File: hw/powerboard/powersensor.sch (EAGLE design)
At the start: 35 parts, among them J1 ISP, J2 I2C

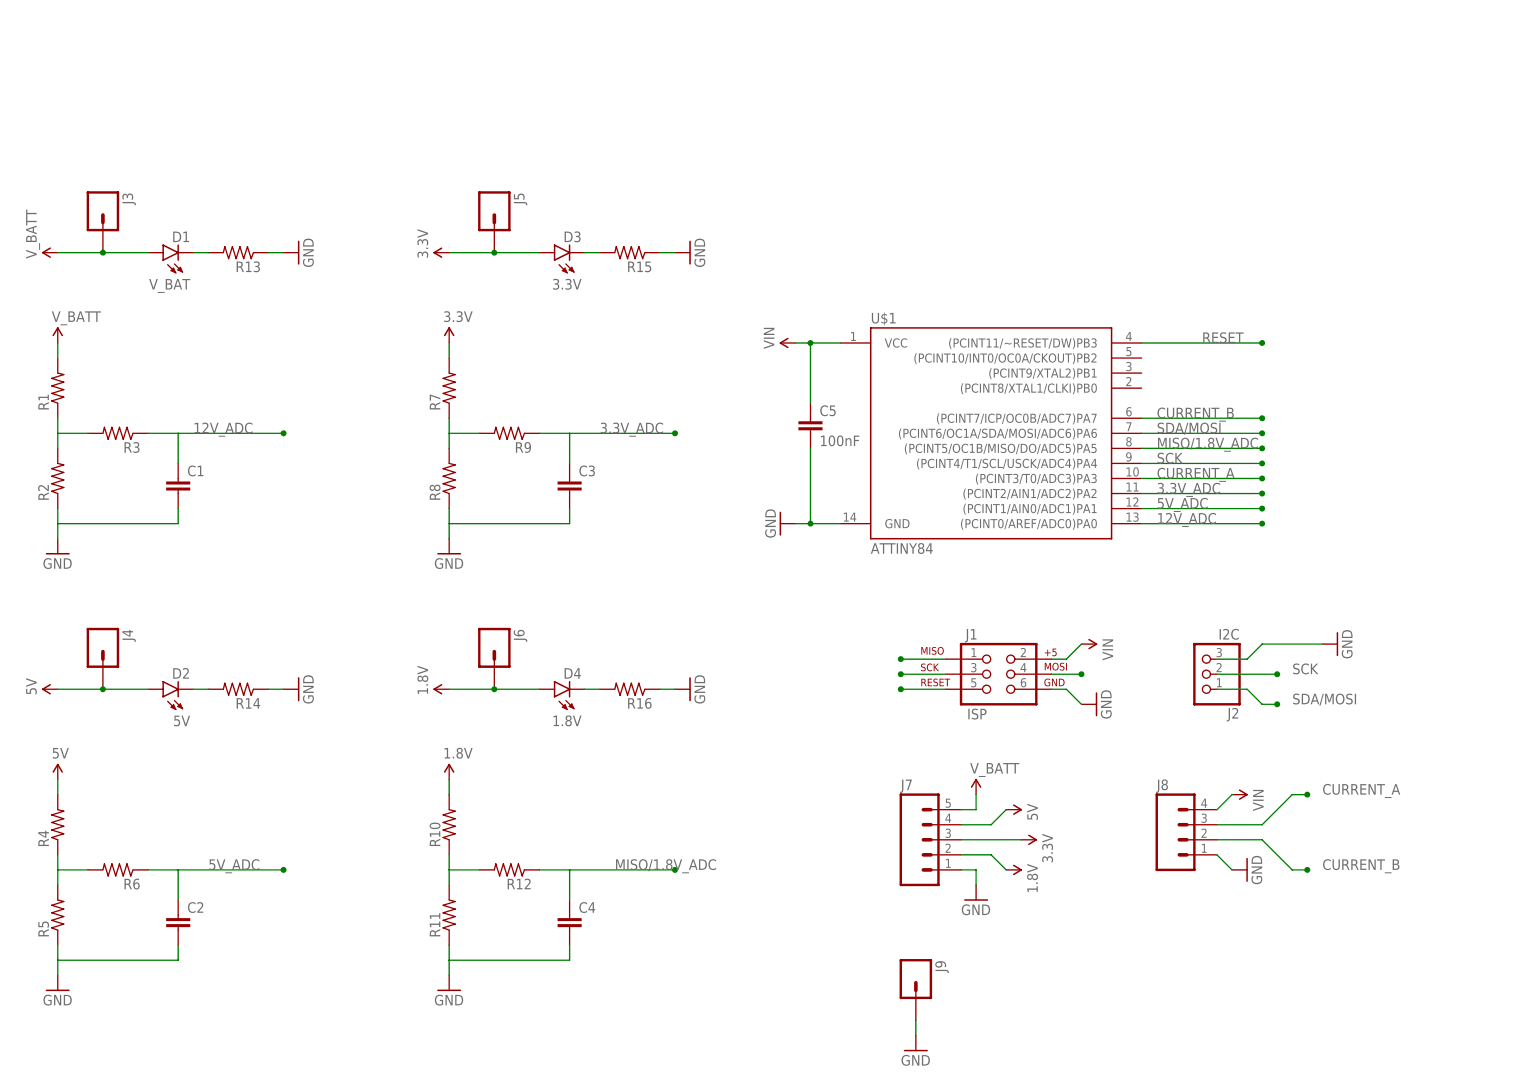
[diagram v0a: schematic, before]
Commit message: Added optional I2C pullups, broke out PB0/1 and performed some cosmetical changes to PowerSensor board
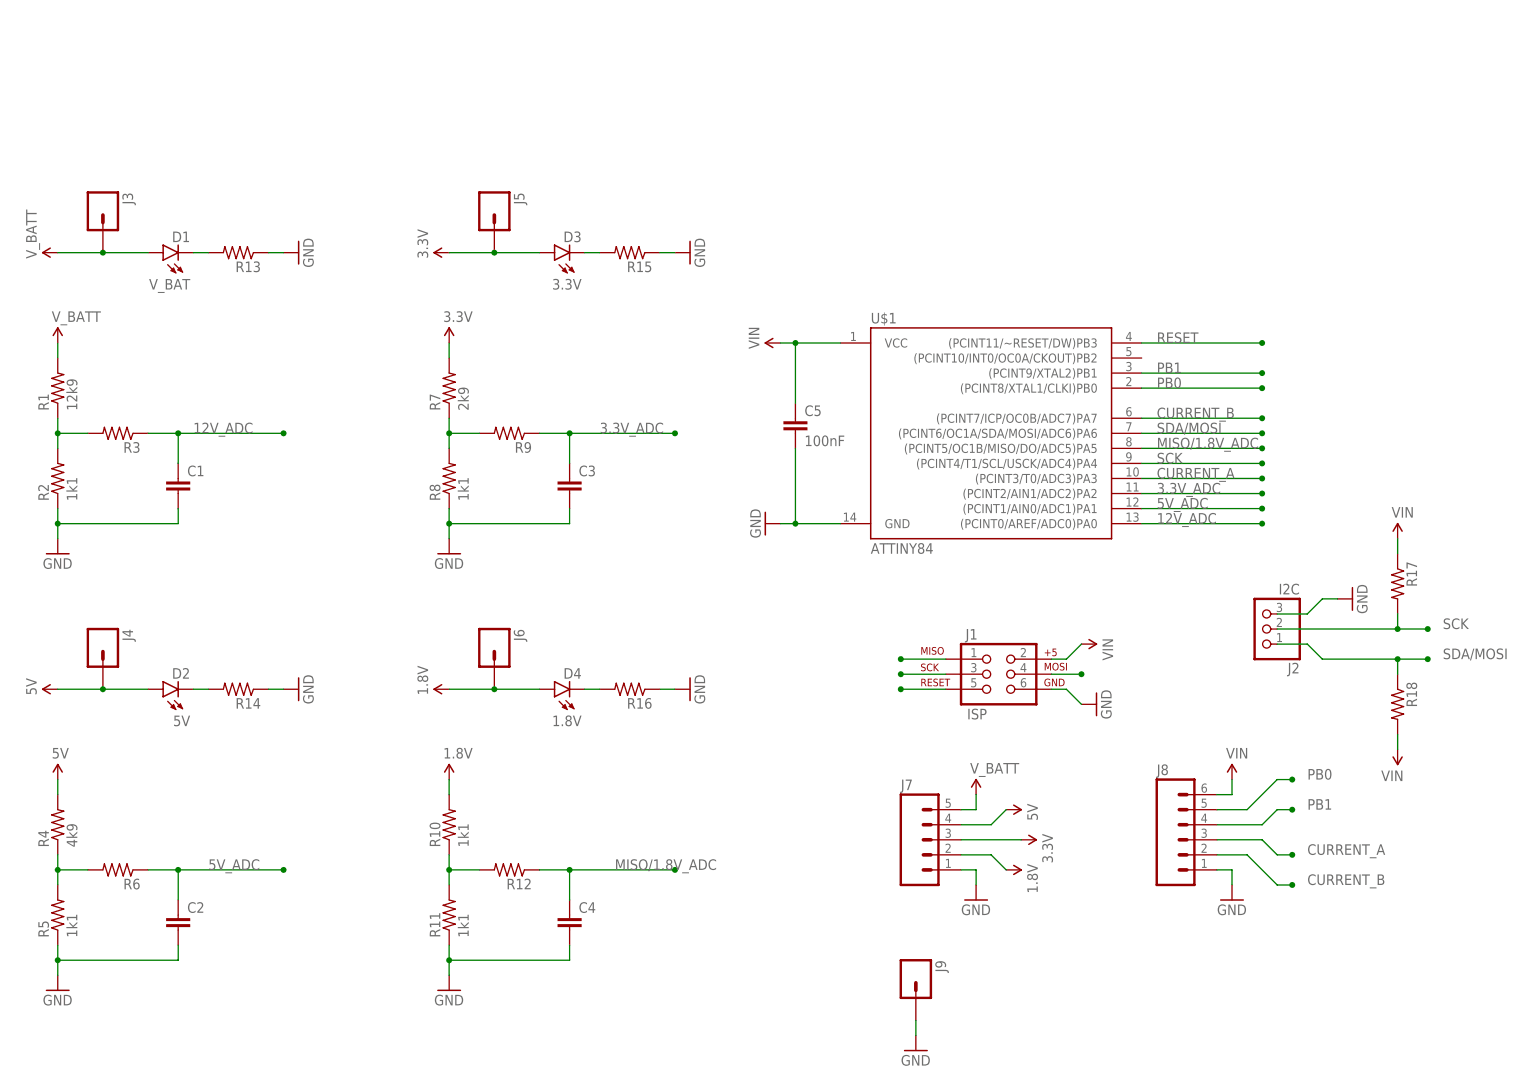
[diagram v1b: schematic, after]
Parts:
- added R17, R18: (no value), SparkFun-Passives:RESISTOR0603-RES
- J8: device SparkFun-Connectors:M04PTH -> SparkFun-Connectors:M06SILK_FEMALE_PTH
- R1: value (none) -> 12k9
- R10, R11, R2, R5, R8: value (none) -> 1k1
- R4: value (none) -> 4k9
- R7: value (none) -> 2k9
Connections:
- new net PB0: J8.5, U$1.(PCINT8/XTAL1/CLKI)PB0
- new net PB1: J8.4, U$1.(PCINT9/XTAL2)PB1
- net SCK: now also R17.2
- net SDA/MOSI: now also R18.1
- net VIN: now also J8.6, R17.1, R18.2; no longer J8.4
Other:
- moved on the sheet: C5, J2

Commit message: Added values and performed some cosmetic changes on PowerSensor schematics
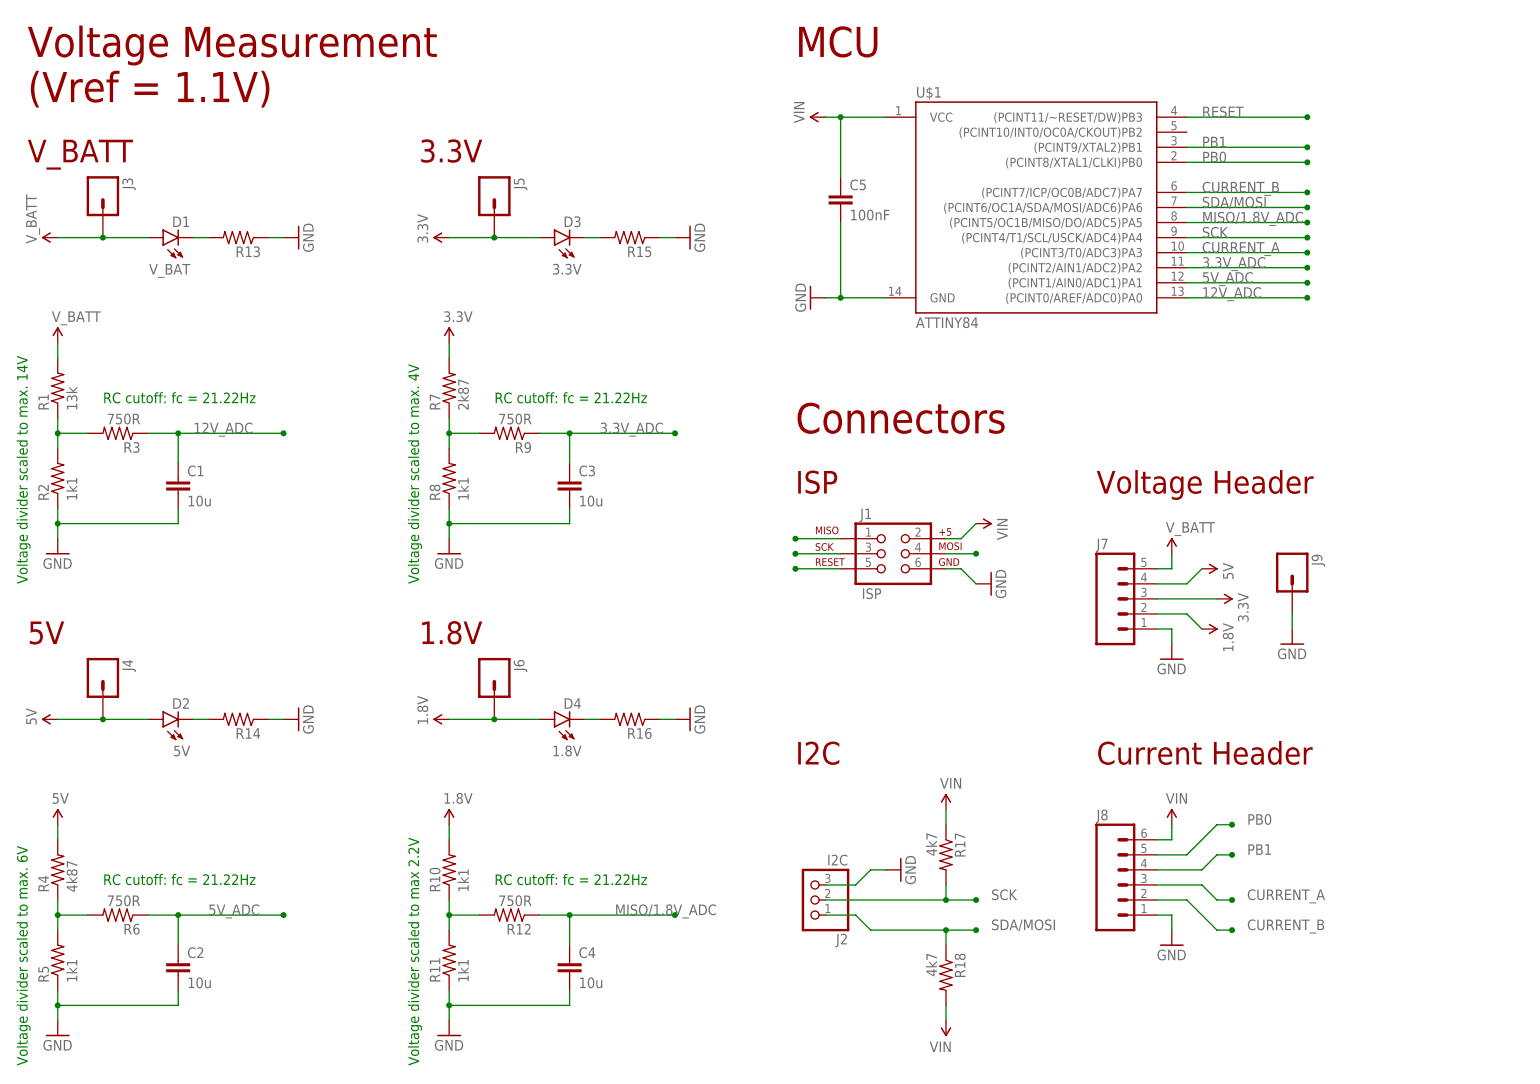
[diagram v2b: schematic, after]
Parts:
- C1, C2, C3, C4: value (none) -> 10u
- R1: value 12k9 -> 13k
- R12, R3, R6, R9: value (none) -> 750R
- R17, R18: value (none) -> 4k7
- R4: value 4k9 -> 4k87
- R7: value 2k9 -> 2k87
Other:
- note added: "1.8V"
- note added: "3.3V"
- note added: "5V"
- note added: "Connectors"
- note added: "Current Header"
- note added: "I2C"
- note added: "ISP"
- note added: "MCU"
- note added: "RC cutoff: fc = 21.22Hz"
- note added: "V_BATT"
- note added: "Voltage Header"
- note added: "Voltage Measurement (Vref = 1.1V)"
- note added: "Voltage divider scaled to max 2.2V"
- note added: "Voltage divider scaled to max. 14V"
- note added: "Voltage divider scaled to max. 4V"
- note added: "Voltage divider scaled to max. 6V"
- moved on the sheet: C2, C4, C5, D1, D2, D3, D4, J1, J2, J3, J4, J5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

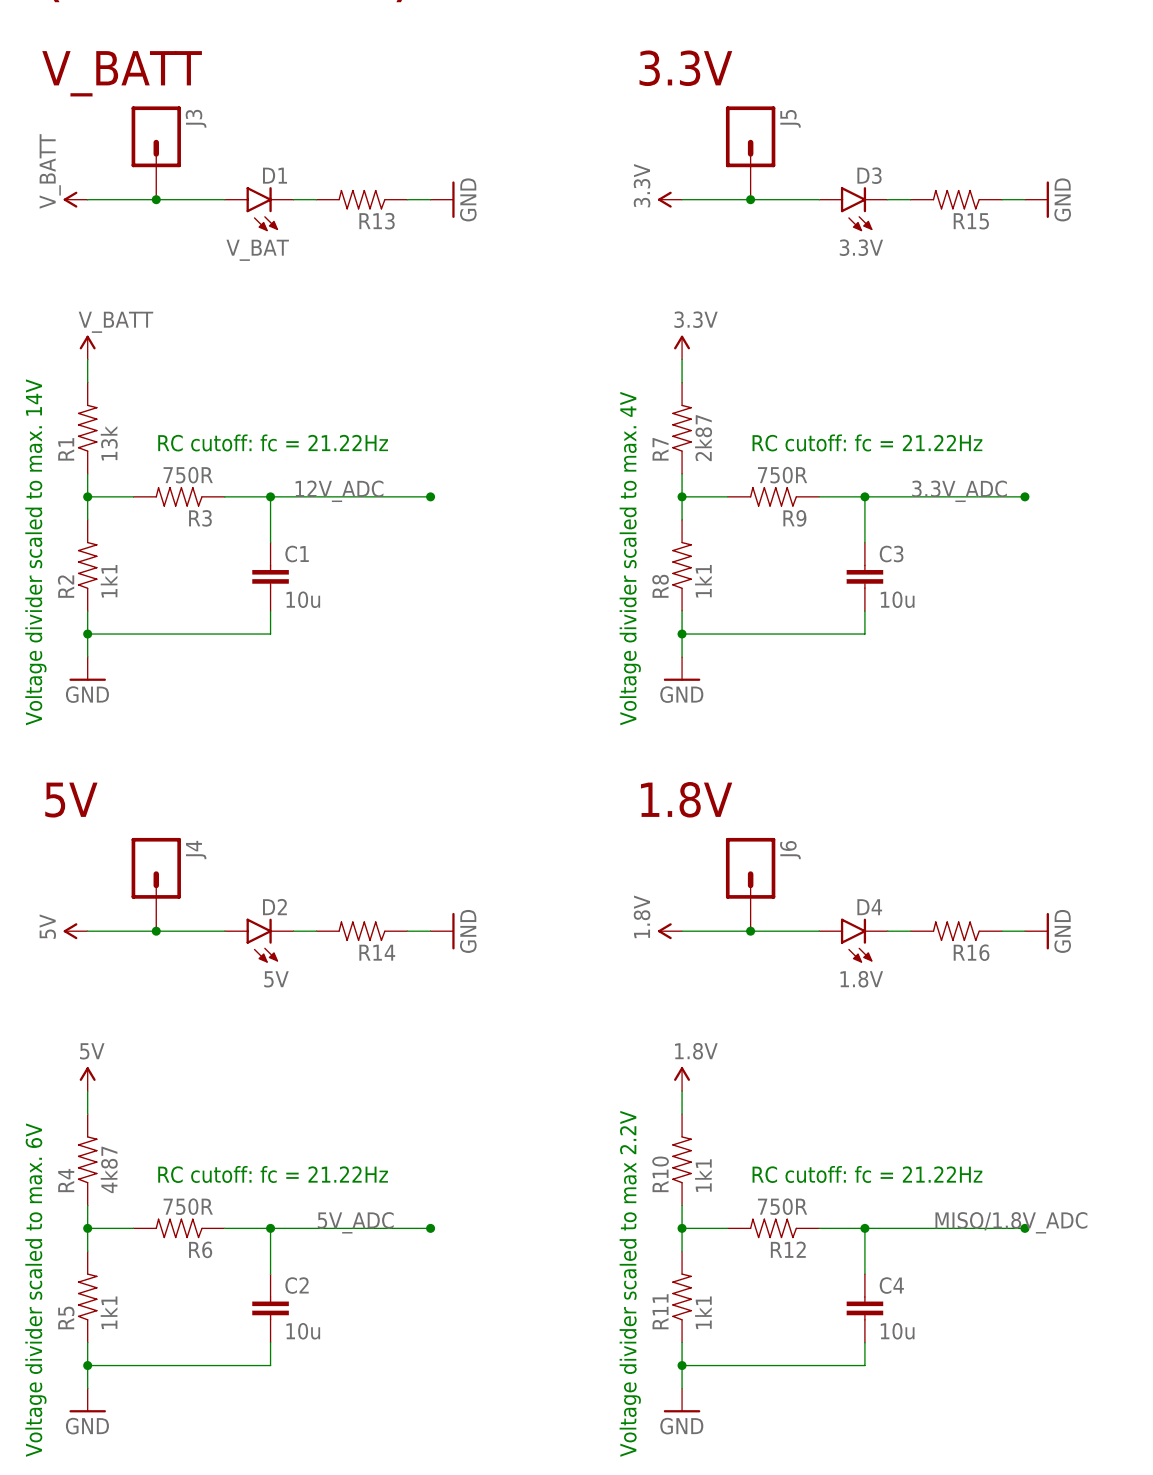
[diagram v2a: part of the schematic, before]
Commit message: Fixed values and added product ids for PowerSensor BOM
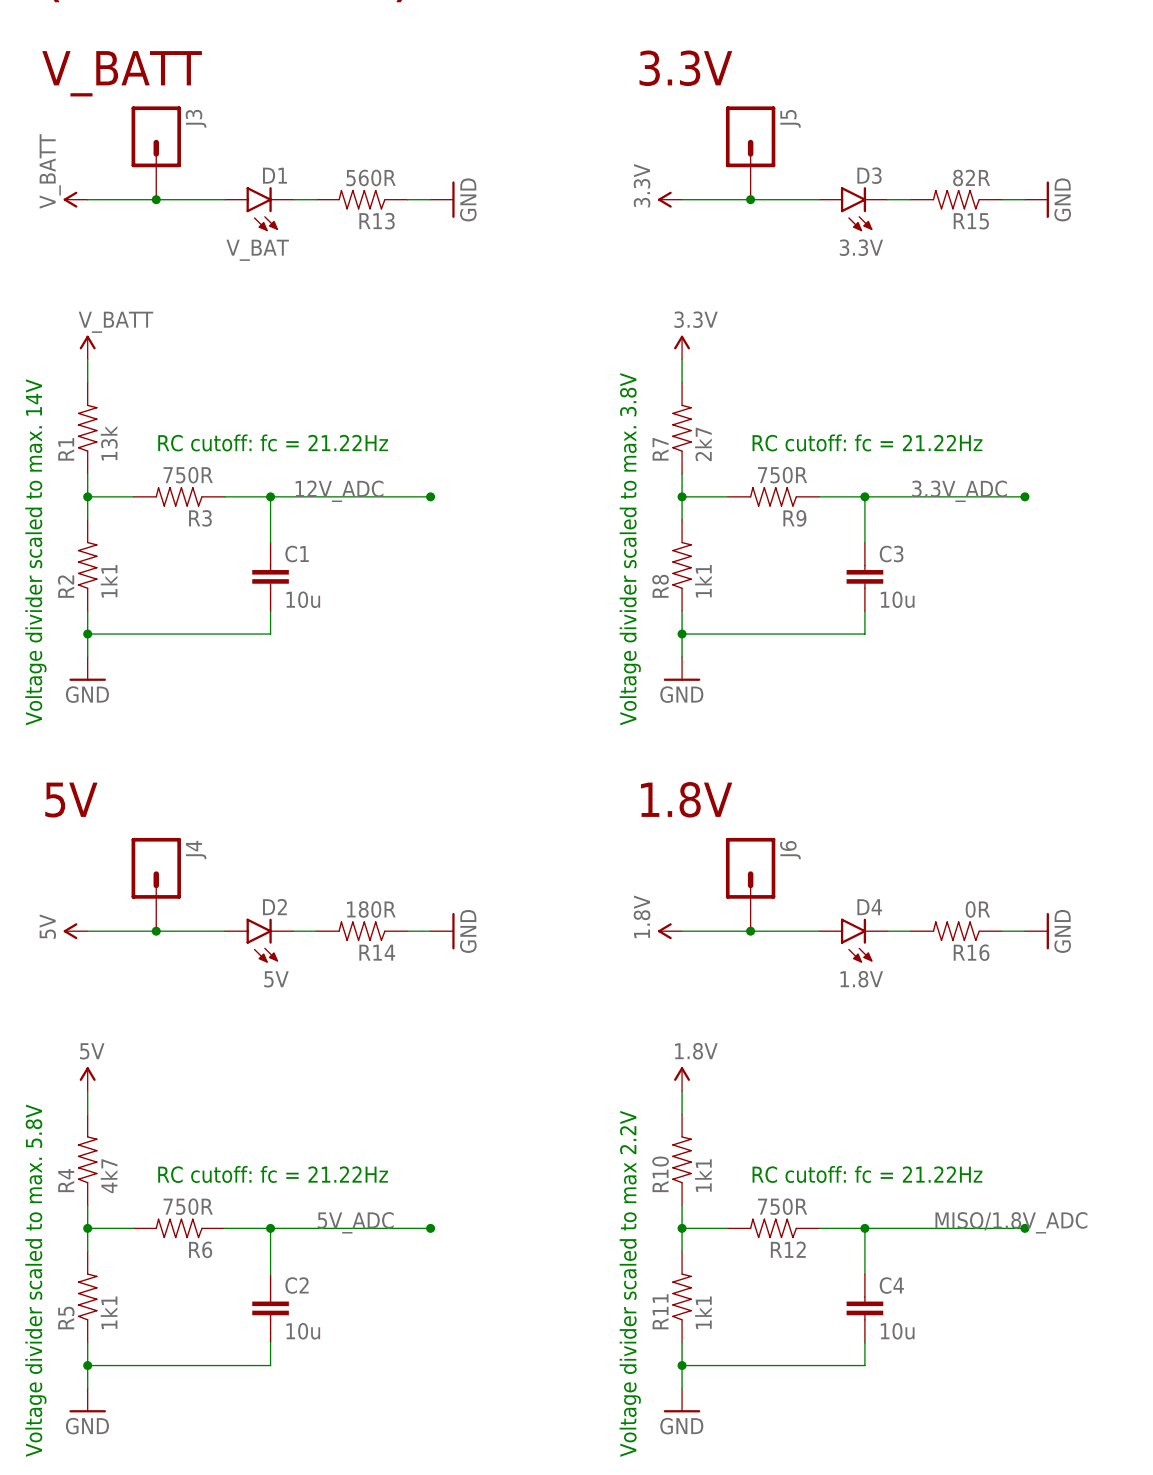
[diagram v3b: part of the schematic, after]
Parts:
- R13: value (none) -> 560R
- R14: value (none) -> 180R
- R15: value (none) -> 82R
- R16: value (none) -> 0R
- R4: value 4k87 -> 4k7
- R7: value 2k87 -> 2k7
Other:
- note added: "Voltage divider scaled to max. 3.8V"
- note added: "Voltage divider scaled to max. 5.8V"
- note removed: "Voltage divider scaled to max. 4V"
- note removed: "Voltage divider scaled to max. 6V"
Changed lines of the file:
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@@
 <part name="GND2" library="SparkFun-Aesthetics" deviceset="GND" device=""/>
 <part name="C1" library="SparkFun-Capacitors" deviceset="CAP" device="0603-CAP" value="10u"/>
-<part name="R4" library="SparkFun-Passives" deviceset="RESISTOR" device="0603-RES" value="4k87"/>
+<part name="R4" library="SparkFun-Passives" deviceset="RESISTOR" device="0603-RES" value="4k7"/>
 <part name="R5" library="SparkFun-Passives" deviceset="RESISTOR" device="0603-RES" value="1k1"/>
 <part name="R6" library="SparkFun-Passives" deviceset="RESISTOR" device="0603-RES" value="750R"/>
 <part name="GND3" library="SparkFun-Aesthetics" deviceset="GND" device=""/>
 <part name="C2" library="SparkFun-Capacitors" deviceset="CAP" device="0603-CAP" value="10u"/>
-<part name="R7" library="SparkFun-Passives" deviceset="RESISTOR" device="0603-RES" value="2k87"/>
+<part name="R7" library="SparkFun-Passives" deviceset="RESISTOR" device="0603-RES" value="2k7"/>
 <part name="R8" library="SparkFun-Passives" deviceset="RESISTOR" device="0603-RES" value="1k1"/>
 <part name="R9" library="SparkFun-Passives" deviceset="RESISTOR" device="0603-RES" value="750R"/>
@@
 <part name="D3" library="SparkFun-LED" deviceset="LED" device="0603" value="3.3V"/>
 <part name="D4" library="SparkFun-LED" deviceset="LED" device="0603" value="1.8V"/>
-<part name="R13" library="SparkFun-Passives" deviceset="RESISTOR" device="0603-RES"/>
-<part name="R14" library="SparkFun-Passives" deviceset="RESISTOR" device="0603-RES"/>
-<part name="R15" library="SparkFun-Passives" deviceset="RESISTOR" device="0603-RES"/>
-<part name="R16" library="SparkFun-Passives" deviceset="RESISTOR" device="0603-RES"/>
+<part name="R13" library="SparkFun-Passives" deviceset="RESISTOR" device="0603-RES" value="560R"/>
+<part name="R14" library="SparkFun-Passives" deviceset="RESISTOR" device="0603-RES" value="180R"/>
+<part name="R15" library="SparkFun-Passives" deviceset="RESISTOR" device="0603-RES" value="82R"/>
+<part name="R16" library="SparkFun-Passives" deviceset="RESISTOR" device="0603-RES" value="0R"/>
 <part name="SUPPLY9" library="SparkFun-Aesthetics" deviceset="5V" device=""/>
 <part name="SUPPLY10" library="SparkFun-Aesthetics" deviceset="3.3V" device=""/>
@@
 <plain>
 <text x="7.62" y="81.28" size="1.778" layer="91" rot="R90">Voltage divider scaled to max. 14V</text>
-<text x="73.66" y="81.28" size="1.778" layer="91" rot="R90">Voltage divider scaled to max. 4V</text>
+<text x="73.66" y="81.28" size="1.778" layer="91" rot="R90">Voltage divider scaled to max. 3.8V</text>
 <text x="73.66" y="0" size="1.778" layer="91" rot="R90">Voltage divider scaled to max 2.2V</text>
-<text x="7.62" y="0" size="1.778" layer="91" rot="R90">Voltage divider scaled to max. 6V</text>
+<text x="7.62" y="0" size="1.778" layer="91" rot="R90">Voltage divider scaled to max. 5.8V</text>
 <text x="7.62" y="152.4" size="3.81" layer="94">V_BATT</text>
 <text x="73.66" y="152.4" size="3.81" layer="94">3.3V</text>
